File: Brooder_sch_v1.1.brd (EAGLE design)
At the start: 80 x 75 mm, 24 parts, among them J1 DCJ0202, J2 1X2-3.5MM, U1 328P

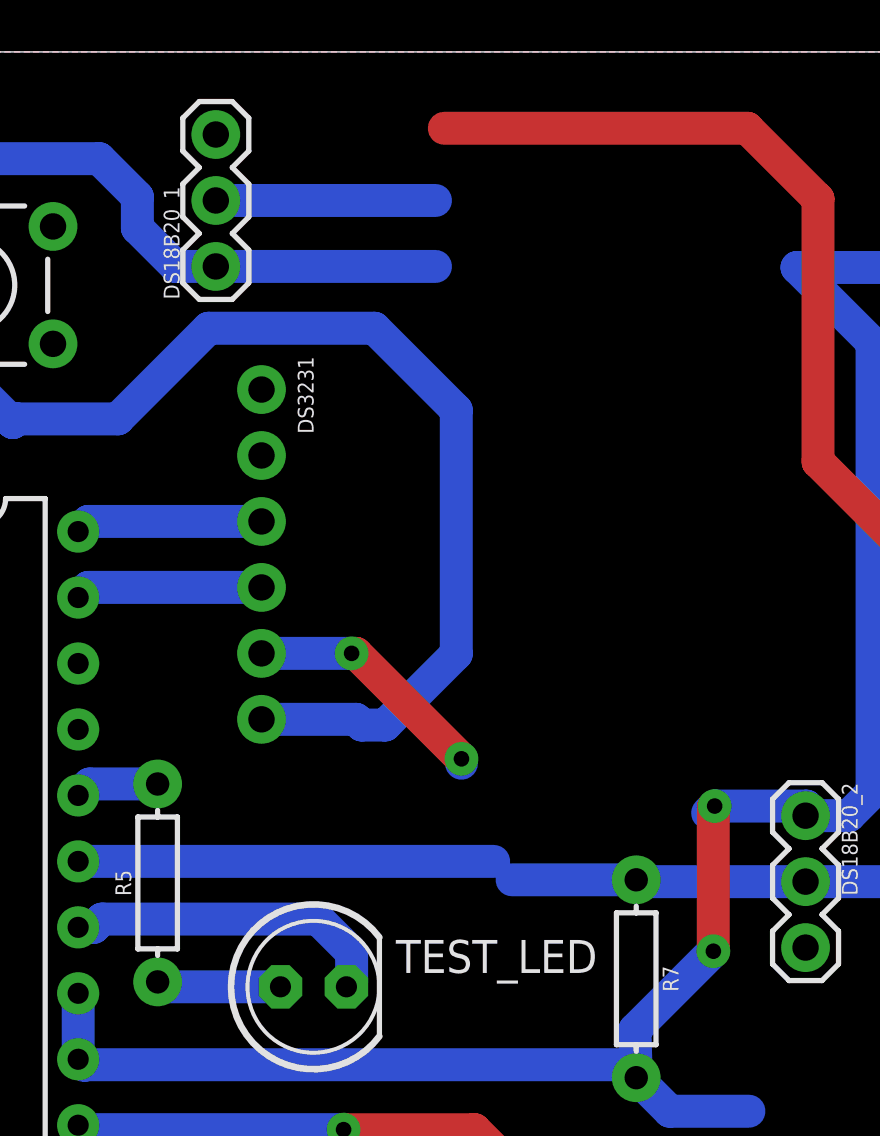
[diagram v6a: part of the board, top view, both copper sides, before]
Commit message: Removes the dht22 resistors
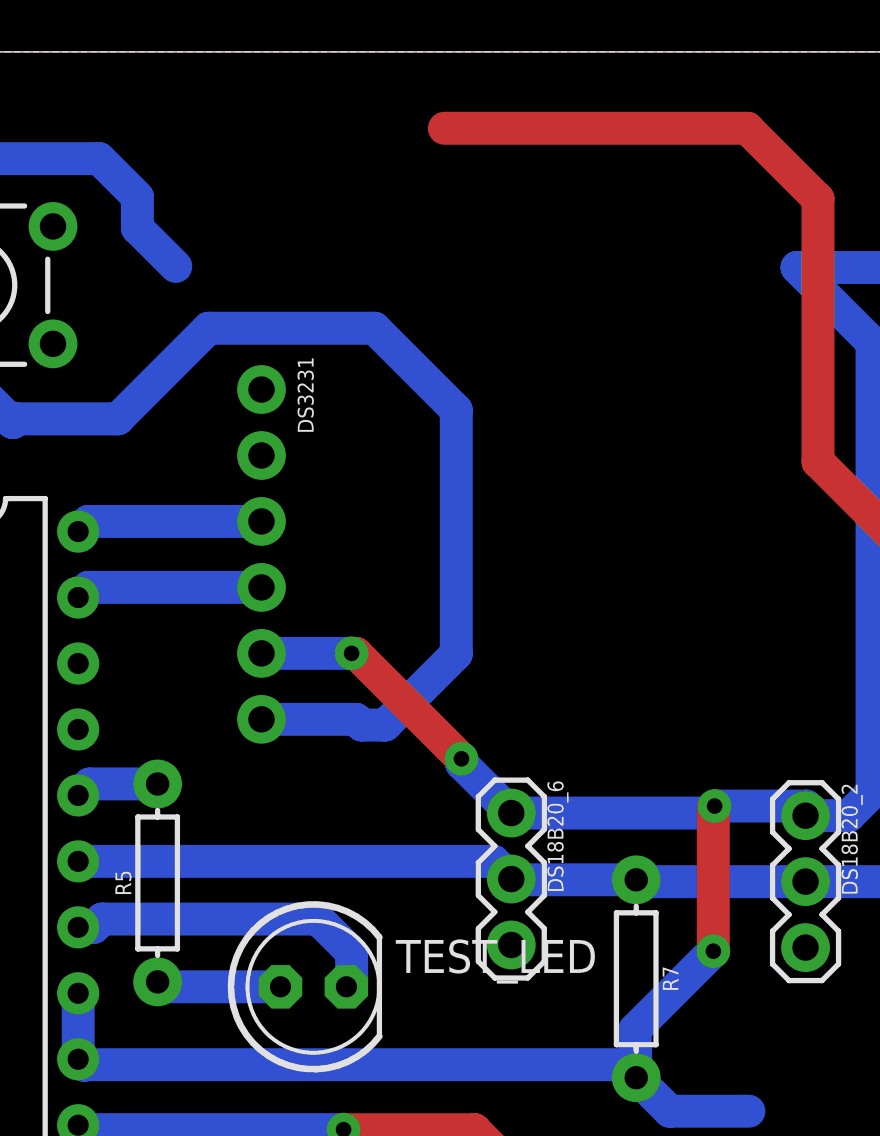
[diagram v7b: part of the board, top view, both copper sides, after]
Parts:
- removed DS18B20_1: 455-1750-1-ND, SparkFun-Connectors:1X03
- added DS18B20_6: 455-1750-1-ND, SparkFun-Connectors:1X03
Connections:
- net 5V: now also DS18B20_6.1; no longer DS18B20_1.1
- net GND: now also DS18B20_6.3; no longer DS18B20_1.3
- net PC0: now also DS18B20_6.2; no longer DS18B20_1.2
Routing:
- net PC0: track 69.0 -> 61.5 mm
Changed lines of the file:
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@@
 <attribute name="PROD_ID" value="XXX-00000" x="69.95" y="45.59" size="1.778" layer="27" rot="R270" display="off"/>
 </element>
-<element name="DS18B20_1" library="SparkFun-Connectors" package="1X03" value="455-1750-1-ND" x="47.24" y="66.74" rot="R90">
-<attribute name="PROD_ID" value="XXX-00000" x="47.24" y="66.74" size="1.778" layer="27" rot="R90" display="off"/>
+<element name="DS18B20_6" library="SparkFun-Connectors" package="1X03" value="455-1750-1-ND" x="58.62" y="45.69" rot="R270">
+<attribute name="PROD_ID" value="XXX-00000" x="58.62" y="45.69" size="1.778" layer="27" rot="R270" display="off"/>
 </element>
 <element name="FTDI" library="SparkFun-Connectors" package="1X06_NO_SILK" value="" x="12.48" y="66.32">
@@
 <contactref element="MICRO_SD" pad="6"/>
 <contactref element="DS18B20_2" pad="3"/>
-<contactref element="DS18B20_1" pad="3"/>
+<contactref element="DS18B20_6" pad="3"/>
 <polygon width="1.27" layer="16" isolate="1.016">
 <vertex x="0" y="0"/>
@@
 <contactref element="U$2" pad="IN(-VE)"/>
 <contactref element="U$2" pad="OUT(-VE)"/>
-<wire x1="46.96" y1="64.36" x2="47.24" y2="71.82" width="0" layer="19" extent="16-16"/>
+<wire x1="76.15" y1="5.46" x2="76.79" y2="16.81" width="0" layer="19" extent="1-1"/>
+<wire x1="63.735740625" y1="1.945340625" x2="76.15" y2="5.46" width="0" layer="19" extent="1-1"/>
 <wire x1="34.32" y1="38.75" x2="41.94" y2="41.29" width="0" layer="19" extent="1-1"/>
 <wire x1="19.71" y1="34.8" x2="19.72" y2="39.62" width="0" layer="19" extent="1-1"/>
-<wire x1="76.15" y1="5.46" x2="63.735740625" y2="1.945340625" width="0" layer="19" extent="1-1"/>
-<wire x1="76.79" y1="16.81" x2="76.15" y2="5.46" width="0" layer="19" extent="1-1"/>
 </signal>
 <signal name="12V">
@@
 <contactref element="DS18B20_2" pad="1"/>
 <contactref element="R7" pad="P$2"/>
-<contactref element="DS18B20_1" pad="1"/>
+<contactref element="DS18B20_6" pad="1"/>
 <wire x1="42.18" y1="35.97" x2="41.94" y2="36.21" width="1.27" layer="16"/>
 <wire x1="41.94" y1="36.21" x2="41.94" y2="38.75" width="1.27" layer="16"/>
@@
 <wire x1="66.45" y1="45.96" x2="69.98" y2="45.96" width="1.27" layer="16"/>
 <wire x1="69.98" y1="45.96" x2="69.95" y2="45.59" width="1.27" layer="16"/>
+<wire x1="58.62" y1="45.69" x2="66.18" y2="45.69" width="1.27" layer="16"/>
 <wire x1="66.18" y1="45.69" x2="66.45" y2="45.96" width="1.27" layer="16"/>
 <wire x1="41.94" y1="36.21" x2="42.15" y2="36" width="1.27" layer="16"/>
@@
 <wire x1="42.15" y1="36" x2="62.93" y2="36" width="1.27" layer="16"/>
 <wire x1="52.47" y1="51.84" x2="49" y2="51.84" width="1.27" layer="16"/>
-<wire x1="47.24" y1="66.74" x2="55.7" y2="66.74" width="1.27" layer="16"/>
 <wire x1="69.62" y1="66.7" x2="74.35" y2="66.7" width="1.27" layer="16"/>
 <wire x1="32.49" y1="20.28" x2="30.92" y2="21.85" width="1.27" layer="1"/>
@@
 <wire x1="44.22" y1="69.42" x2="44.22" y2="68.22" width="1.27" layer="16"/>
 <wire x1="44.22" y1="68.22" x2="45.7" y2="66.74" width="1.27" layer="16"/>
-<wire x1="45.7" y1="66.74" x2="47.24" y2="66.74" width="1.27" layer="16"/>
 <wire x1="42.75" y1="70.89" x2="44.22" y2="69.42" width="1.27" layer="16"/>
 <wire x1="69.95" y1="45.59" x2="71.62" y2="45.59" width="1.27" layer="16"/>
@@
 <wire x1="64.72" y1="34.21" x2="63.43" y2="35.5" width="1.27" layer="16"/>
 <wire x1="32.49" y1="15.23" x2="32.49" y2="20.28" width="1.27" layer="1"/>
+<wire x1="58.62" y1="45.69" x2="56.7" y2="47.61" width="1.27" layer="16"/>
 <wire x1="56.7" y1="47.61" x2="56.7" y2="47.78" width="1.27" layer="16"/>
 <via x="56.7" y="47.78" extent="1-16" drill="0.6" diameter="1.3"/>
@@
 <wire x1="11.58" y1="23.46" x2="16.33" y2="30.95" width="0" layer="19" extent="1-1"/>
 <wire x1="4.19" y1="19.93" x2="4.31" y2="27.47" width="0" layer="19" extent="1-1"/>
-<wire x1="56.7" y1="47.61" x2="66.18" y2="45.69" width="0" layer="19" extent="16-16"/>
 <wire x1="63.74" y1="19.72" x2="64.72" y2="34.21" width="0" layer="19" extent="16-16"/>
 <wire x1="69.35" y1="10.67" x2="63.74" y2="19.72" width="0" layer="19" extent="1-1"/>
@@
 <signal name="PC0">
 <contactref element="U1" pad="23"/>
-<contactref element="DS18B20_1" pad="2"/>
 <contactref element="R7" pad="P$1"/>
 <contactref element="DS18B20_2" pad="2"/>
+<contactref element="DS18B20_6" pad="2"/>
 <wire x1="41.94" y1="43.83" x2="57.94" y2="43.83" width="1.27" layer="16"/>
+<wire x1="57.94" y1="43.83" x2="58.62" y2="43.15" width="1.27" layer="16"/>
+<wire x1="58.62" y1="43.15" x2="58.65" y2="43.12" width="1.27" layer="16"/>
 <wire x1="58.65" y1="43.12" x2="63.43" y2="43.12" width="1.27" layer="16"/>
 <wire x1="63.43" y1="43.12" x2="63.5" y2="43.05" width="1.27" layer="16"/>
 <wire x1="63.5" y1="43.05" x2="69.95" y2="43.05" width="1.27" layer="16"/>
-<wire x1="47.24" y1="69.28" x2="55.7" y2="69.28" width="1.27" layer="16"/>
 <wire x1="76.87" y1="69.23" x2="77.4" y2="68.7" width="1.27" layer="16"/>
 <wire x1="77.4" y1="68.7" x2="77.4" y2="44.19" width="1.27" layer="16"/>
 <wire x1="76.26" y1="43.05" x2="69.95" y2="43.05" width="1.27" layer="16"/>
 <wire x1="77.4" y1="44.19" x2="76.26" y2="43.05" width="1.27" layer="16"/>
-<wire x1="76.87" y1="69.23" x2="55.7" y2="69.28" width="0" layer="19" extent="16-16"/>
-<wire x1="57.94" y1="43.83" x2="58.65" y2="43.12" width="0" layer="19" extent="16-16"/>
 </signal>
 <signal name="PB2">

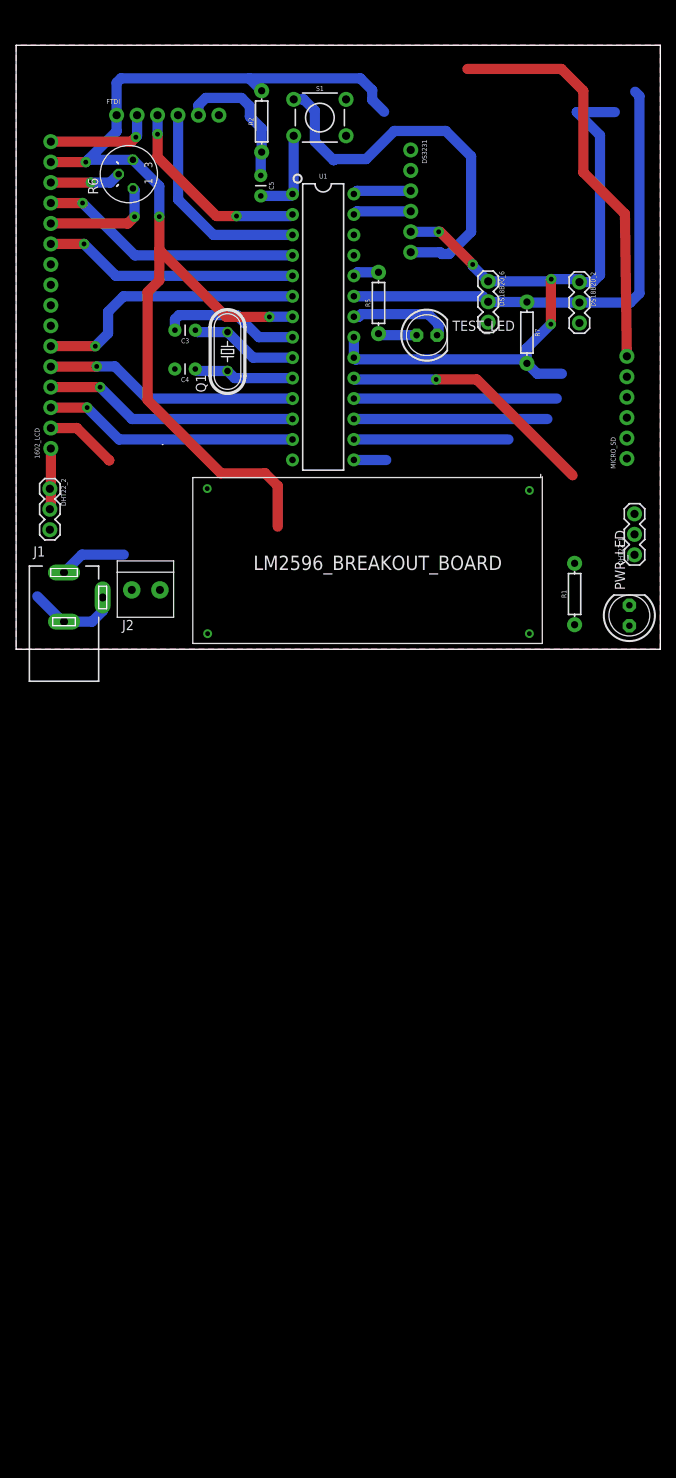
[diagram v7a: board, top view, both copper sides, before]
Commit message: Adds the sim800l V2 pin headers
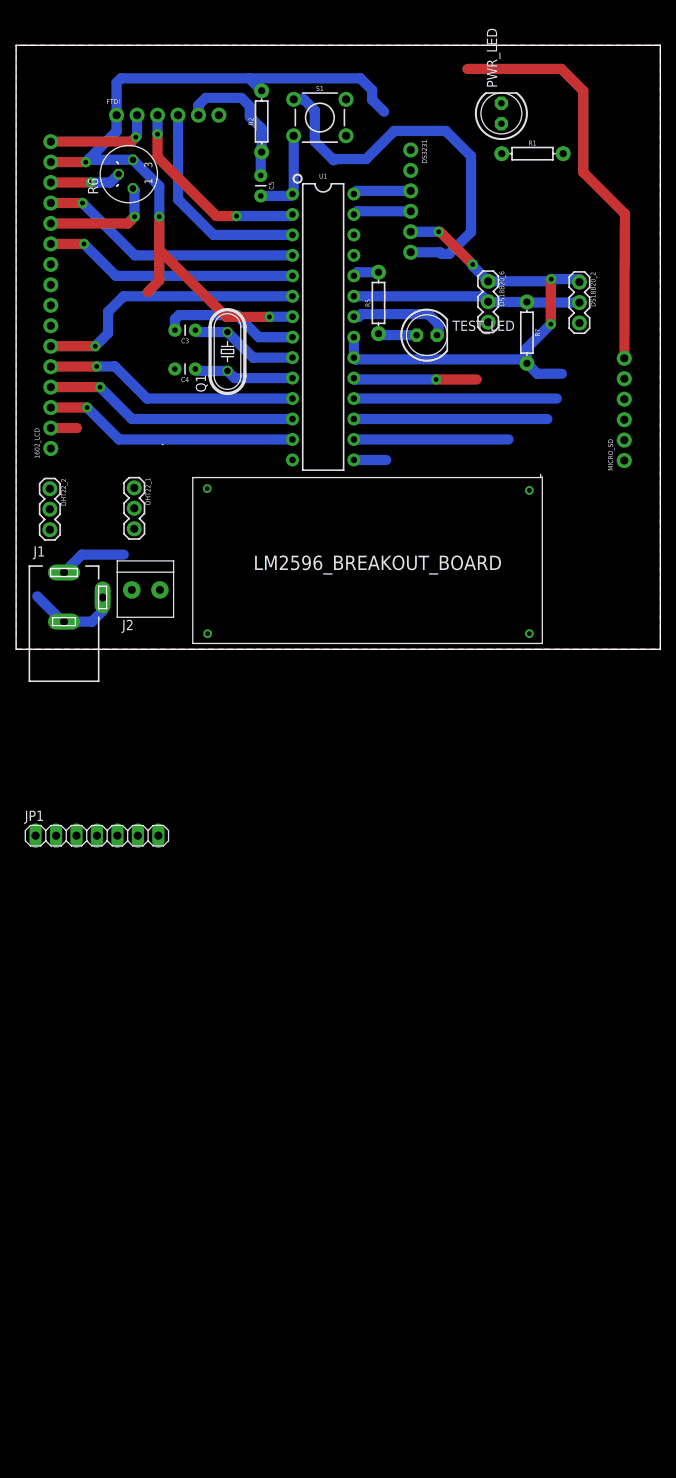
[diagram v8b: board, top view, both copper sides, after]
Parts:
- added JP1: (no value), pinhead:1X07
- moved PWR_LED 64.3 mm to (60.3, 66.5)
- moved DHT22_1 62.7 mm to (14.7, 20.0), turned to 270 degrees
- moved R1 54.9 mm to (64.1, 61.5), turned to 0 degrees
- moved MICRO_SD 0.41 mm to (75.5, 23.4)
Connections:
- new net N$12: JP1.7
- new net RX: JP1.5, U1.26
- new net TX: JP1.4, U1.25
- net 5V: now also JP1.1, JP1.3
- net GND: now also JP1.2, JP1.6
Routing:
- net 5V: track 240.7 -> 166.9 mm
- net PC0: track 61.5 -> 28.3 mm
- net PB5: track 32.2 -> 15.3 mm
- net GND: track 175.3 -> 168.7 mm
